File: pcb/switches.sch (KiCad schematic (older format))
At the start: 54 parts, among them SW1 SW_Push, SW10 EN_01, SW11 EN_02, SW12 EN_03, SW2 SW_Push, SW3 SW_Push, SW4 SW_Push, SW5 SW_Push, SW6 SW_Push, SW7 SW_Push, SW8 SW_Push, SW9 SW_Push

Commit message: Components positioning
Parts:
- removed SW10: EN_01, Rotary_Encoder:RotaryEncoder_Alps_EC11E-Switch_Vertical_H20mm_CircularMountingHoles, symbol Device:Rotary_Encoder_Switch
- added J5: Conn_01x05_Male, Connector_PinHeader_2.54mm:PinHeader_1x05_P2.54mm_Horizontal, symbol Connector:Conn_01x05_Male
- renumbered SW11 to ENC2, SW12 to ENC3
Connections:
- net ENC_01_A: now also J5.2 (Pin_2)
- net ENC_01_B: now also J5.1 (Pin_1)
- net GND: now also J5.4 (Pin_4), J5.5 (Pin_5)
- net at C22.1, R33.2, R36.1: now also J5.3 (Pin_3)
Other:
- moved on the sheet: R27, R28
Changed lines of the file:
@@
 	7500 3800 7500 3950
-$Comp
-L Device:Rotary_Encoder_Switch SW?
-U 1 1 61BDCAD5
-P 2600 5550
-AR Path="/61BDCAD5" Ref="SW?"  Part="1"
-AR Path="/61B99CE8/61BDCAD5" Ref="SW10"  Part="1"
-F 0 "SW10" H 2600 5900 50  0000 C CNN
-F 1 "EN_01" H 2650 5800 50  0000 C CNN
-F 2 "Rotary_Encoder:RotaryEncoder_Alps_EC11E-Switch_Vertical_H20mm_CircularMountingHoles" H 2450 5710 50  0001 C CNN
-F 3 "~" H 2600 5810 50  0001 C CNN
-	1    2600 5550
-	1    0    0    -1
-$EndComp
-$Comp
-L power:GND #PWR?
-U 1 1 61BDCADB
-P 1500 5550
-AR Path="/61BDCADB" Ref="#PWR?"  Part="1"
-AR Path="/61B99CE8/61BDCADB" Ref="#PWR064"  Part="1"
-F 0 "#PWR064" H 1500 5300 50  0001 C CNN
-F 1 "GND" H 1505 5377 50  0000 C CNN
-F 2 "" H 1500 5550 50  0001 C CNN
-F 3 "" H 1500 5550 50  0001 C CNN
-	1    1500 5550
-	1    0    0    -1
-$EndComp
 $Comp
 L Device:R R?
@@
 Wire Wire Line
 	3200 5800 3200 5950
-Wire Wire Line
-	2900 5450 3200 5450
 Text GLabel 3650 5450 2    50   Output ~ 0
 ENC_01_btn
@@
 L power:GND #PWR?
 U 1 1 61BDCB08
-P 2900 5950
+P 2780 6040
 AR Path="/61BDCB08" Ref="#PWR?"  Part="1"
 AR Path="/61B99CE8/61BDCB08" Ref="#PWR067"  Part="1"
-F 0 "#PWR067" H 2900 5700 50  0001 C CNN
-F 1 "GND" H 2905 5777 50  0000 C CNN
-F 2 "" H 2900 5950 50  0001 C CNN
-F 3 "" H 2900 5950 50  0001 C CNN
-	1    2900 5950
-	1    0    0    -1
-$EndComp
-Text GLabel 2050 5450 0    50   Output ~ 0
+F 0 "#PWR067" H 2780 5790 50  0001 C CNN
+F 1 "GND" H 2785 5867 50  0000 C CNN
+F 2 "" H 2780 6040 50  0001 C CNN
+F 3 "" H 2780 6040 50  0001 C CNN
+	1    2780 6040
+	1    0    0    -1
+$EndComp
+Text GLabel 2520 5090 0    50   Output ~ 0
 ENC_01_A
-Text GLabel 2050 5650 0    50   Output ~ 0
+Text GLabel 2520 5290 0    50   Output ~ 0
 ENC_01_B
 $Comp
 L Device:R R?
 U 1 1 61BDCB10
-P 2250 5200
+P 2720 4840
 AR Path="/61BDCB10" Ref="R?"  Part="1"
 AR Path="/61B99CE8/61BDCB10" Ref="R28"  Part="1"
-F 0 "R28" V 2350 5050 50  0000 C CNN
-F 1 "R" V 2350 5150 50  0000 C CNN
-F 2 "Resistor_SMD:R_0603_1608Metric" V 2180 5200 50  0001 C CNN
-F 3 "~" H 2250 5200 50  0001 C CNN
-	1    2250 5200
-	1    0    0    -1
-$EndComp
-Wire Wire Line
-	2250 5350 2250 5450
-Connection ~ 2250 5450
-Wire Wire Line
-	2250 5450 2300 5450
+F 0 "R28" V 2820 4690 50  0000 C CNN
+F 1 "R" V 2820 4790 50  0000 C CNN
+F 2 "Resistor_SMD:R_0603_1608Metric" V 2650 4840 50  0001 C CNN
+F 3 "~" H 2720 4840 50  0001 C CNN
+	1    2720 4840
+	1    0    0    -1
+$EndComp
+Wire Wire Line
+	2720 4990 2720 5090
+Connection ~ 2720 5090
 $Comp
 L Device:R R?
 U 1 1 61BDCB19
-P 2100 5200
+P 2570 4840
 AR Path="/61BDCB19" Ref="R?"  Part="1"
 AR Path="/61B99CE8/61BDCB19" Ref="R27"  Part="1"
-F 0 "R27" V 2200 5300 50  0000 C CNN
-F 1 "R" V 2200 5200 50  0000 C CNN
-F 2 "Resistor_SMD:R_0603_1608Metric" V 2030 5200 50  0001 C CNN
-F 3 "~" H 2100 5200 50  0001 C CNN
-	1    2100 5200
+F 0 "R27" V 2670 4940 50  0000 C CNN
+F 1 "R" V 2670 4840 50  0000 C CNN
+F 2 "Resistor_SMD:R_0603_1608Metric" V 2500 4840 50  0001 C CNN
+F 3 "~" H 2570 4840 50  0001 C CNN
+	1    2570 4840
 	-1   0    0    1
 $EndComp
 Wire Wire Line
-	2050 5450 2250 5450
-Wire Wire Line
-	2100 5350 2100 5650
-Wire Wire Line
-	2100 5650 2050 5650
-Connection ~ 2100 5650
-Wire Wire Line
-	2100 5650 2300 5650
-Wire Wire Line
-	1500 5550 2300 5550
+	2520 5090 2720 5090
+Wire Wire Line
+	2570 4990 2570 5290
+Wire Wire Line
+	2570 5290 2520 5290
+Connection ~ 2570 5290
+Wire Wire Line
+	2570 5290 2770 5290
 $Comp
 L power:+3.3V #PWR?
 U 1 1 61BDCB25
-P 2200 5000
+P 2670 4640
 AR Path="/61BDCB25" Ref="#PWR?"  Part="1"
 AR Path="/61B99CE8/61BDCB25" Ref="#PWR058"  Part="1"
-F 0 "#PWR058" H 2200 4850 50  0001 C CNN
-F 1 "+3.3V" H 2215 5173 50  0000 C CNN
-F 2 "" H 2200 5000 50  0001 C CNN
-F 3 "" H 2200 5000 50  0001 C CNN
-	1    2200 5000
-	1    0    0    -1
-$EndComp
-Wire Wire Line
-	2100 5050 2200 5050
-Wire Wire Line
-	2200 5050 2200 5000
-Wire Wire Line
-	2200 5050 2250 5050
-Connection ~ 2200 5050
-Wire Wire Line
-	2900 5650 2900 5950
+F 0 "#PWR058" H 2670 4490 50  0001 C CNN
+F 1 "+3.3V" H 2685 4813 50  0000 C CNN
+F 2 "" H 2670 4640 50  0001 C CNN
+F 3 "" H 2670 4640 50  0001 C CNN
+	1    2670 4640
+	1    0    0    -1
+$EndComp
+Wire Wire Line
+	2570 4690 2670 4690
+Wire Wire Line
+	2670 4690 2670 4640
+Wire Wire Line
+	2670 4690 2720 4690
+Connection ~ 2670 4690
 $Comp
 L Device:Rotary_Encoder_Switch SW?
@@
 P 5550 5550
 AR Path="/61BDCB30" Ref="SW?"  Part="1"
-AR Path="/61B99CE8/61BDCB30" Ref="SW11"  Part="1"
-F 0 "SW11" H 5550 5900 50  0000 C CNN
+AR Path="/61B99CE8/61BDCB30" Ref="ENC2"  Part="1"
+F 0 "ENC2" H 5550 5900 50  0000 C CNN
 F 1 "EN_02" H 5600 5800 50  0000 C CNN
 F 2 "Rotary_Encoder:RotaryEncoder_Alps_EC11E-Switch_Vertical_H20mm_CircularMountingHoles" H 5400 5710 50  0001 C CNN
@@
 P 8600 5550
 AR Path="/61BDCB8B" Ref="SW?"  Part="1"
-AR Path="/61B99CE8/61BDCB8B" Ref="SW12"  Part="1"
-F 0 "SW12" H 8600 5900 50  0000 C CNN
+AR Path="/61B99CE8/61BDCB8B" Ref="ENC3"  Part="1"
+F 0 "ENC3" H 8600 5900 50  0000 C CNN
 F 1 "EN_03" H 8650 5800 50  0000 C CNN
 F 2 "Rotary_Encoder:RotaryEncoder_Alps_EC11E-Switch_Vertical_H20mm_CircularMountingHoles" H 8450 5710 50  0001 C CNN
@@
 	1    0    0    -1
 $EndComp
+$Comp
+L Connector:Conn_01x05_Male J5
+U 1 1 61E13F1C
+P 2450 5740
+F 0 "J5" H 2090 5840 50  0000 C CNN
+F 1 "Conn_01x05_Male" H 2080 5740 50  0000 C CNN
+F 2 "Connector_PinHeader_2.54mm:PinHeader_1x05_P2.54mm_Horizontal" H 2450 5740 50  0001 C CNN
+F 3 "~" H 2450 5740 50  0001 C CNN
+	1    2450 5740
+	1    0    0    -1
+$EndComp
+Wire Wire Line
+	2650 5840 2780 5840
+Wire Wire Line
+	2780 5840 2780 5940
+Wire Wire Line
+	2650 5940 2780 5940
+Connection ~ 2780 5940
+Wire Wire Line
+	2780 5940 2780 6040
+Wire Wire Line
+	2650 5740 3030 5740
+Wire Wire Line
+	3030 5740 3030 5450
+Wire Wire Line
+	3030 5450 3200 5450
+Wire Wire Line
+	2920 5090 2920 5640
+Wire Wire Line
+	2920 5640 2650 5640
+Wire Wire Line
+	2720 5090 2920 5090
+Wire Wire Line
+	2770 5290 2770 5540
+Wire Wire Line
+	2770 5540 2650 5540
 $EndSCHEMATC

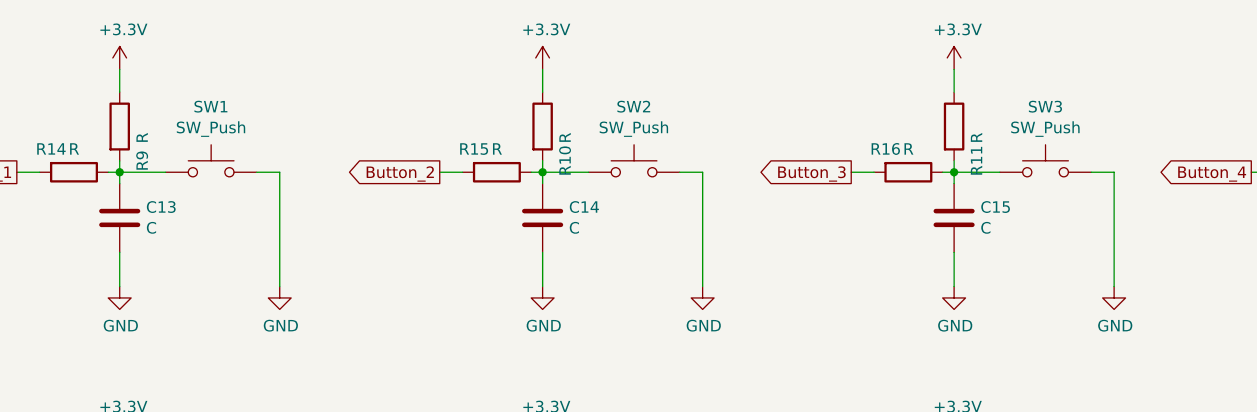
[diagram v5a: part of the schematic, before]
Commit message: Components placement, added 3d model of cherry mx switch
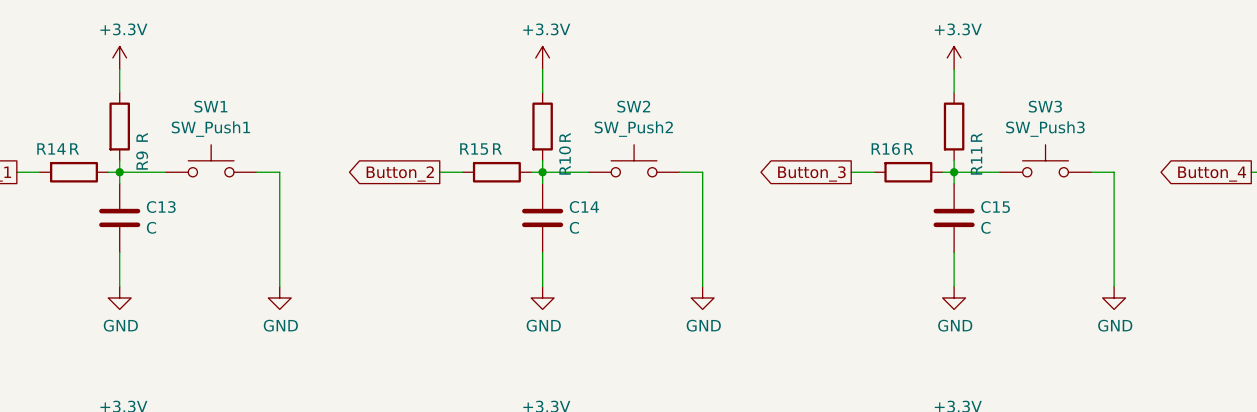
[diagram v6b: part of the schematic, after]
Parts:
- SW1: value SW_Push -> SW_Push1
- SW2: value SW_Push -> SW_Push2
- SW3: value SW_Push -> SW_Push3
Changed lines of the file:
@@
 P 2500 1800
 F 0 "SW1" H 2500 2085 50  0000 C CNN
-F 1 "SW_Push" H 2500 1994 50  0000 C CNN
+F 1 "SW_Push1" H 2500 1994 50  0000 C CNN
 F 2 "Button_Switch_Keyboard:SW_Cherry_MX_1.00u_PCB" H 2500 2000 50  0001 C CNN
 F 3 "~" H 2500 2000 50  0001 C CNN
 	1    2500 1800
-	1    0    0    -1
-$EndComp
-$Comp
-L Switch:SW_Push SW2
-U 1 1 61FC48AC
-P 4350 1800
-F 0 "SW2" H 4350 2085 50  0000 C CNN
-F 1 "SW_Push" H 4350 1994 50  0000 C CNN
-F 2 "Button_Switch_Keyboard:SW_Cherry_MX_1.00u_PCB" H 4350 2000 50  0001 C CNN
-F 3 "~" H 4350 2000 50  0001 C CNN
-	1    4350 1800
 	1    0    0    -1
 $EndComp
@@
 P 6150 1800
 F 0 "SW3" H 6150 2085 50  0000 C CNN
-F 1 "SW_Push" H 6150 1994 50  0000 C CNN
+F 1 "SW_Push3" H 6150 1994 50  0000 C CNN
 F 2 "Button_Switch_Keyboard:SW_Cherry_MX_1.00u_PCB" H 6150 2000 50  0001 C CNN
 F 3 "~" H 6150 2000 50  0001 C CNN
@@
 Wire Wire Line
 	2770 5540 2650 5540
+$Comp
+L Switch:SW_Push SW2
+U 1 1 61FC48AC
+P 4350 1800
+F 0 "SW2" H 4350 2085 50  0000 C CNN
+F 1 "SW_Push2" H 4350 1994 50  0000 C CNN
+F 2 "Button_Switch_Keyboard:SW_Cherry_MX_1.00u_PCB" H 4350 2000 50  0001 C CNN
+F 3 "~" H 4350 2000 50  0001 C CNN
+	1    4350 1800
+	1    0    0    -1
+$EndComp
 $EndSCHEMATC
